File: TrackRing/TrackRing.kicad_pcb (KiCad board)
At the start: 2 copper layers, 12 x 15 mm, 7 parts, among them J1 Conn_01x04, U1 TLV493D-A1B6

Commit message: Finished BusChain PCB
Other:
- board text added: "TrackRing 1.1"
- board text added: "©CGR"
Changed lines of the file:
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@@
+    (effects (font (size 1 1) (thickness 0.15)) (justify left bottom mirror))
+  )
+  (gr_text "©CGR" (at 30.3 23.3) (layer "B.SilkS")
     (effects (font (size 1 1) (thickness 0.15)) (justify left bottom mirror))
   )
@@
     (effects (font (size 1 1) (thickness 0.15)) (justify left bottom mirror))
   )
+  (gr_text "TrackRing 1.1" (at 31.1 21.7) (layer "B.SilkS")
+    (effects (font (size 1 1) (thickness 0.15)) (justify left bottom mirror))
+  )

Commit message: Finalized PCBs for fabrication
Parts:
- added D1: LED, LED_SMD:LED_0603_1608Metric, F.Cu at (30.0, 32.0)
- added R5: 500, Resistor_SMD:R_0402_1005Metric, F.Cu at (31.5, 32.5)
- moved R3 1.01 mm to (28.5, 31.5)
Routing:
- net Net-(D1-K): track 0.00 -> 1.59 mm
- net /VCC: track 14.5 -> 15.5 mm
- net /SDA: track 9.33 -> 8.30 mm
- net GND: track 5.30 -> 6.29 mm, vias 4 -> 5
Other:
- board text added: "TrackRing 1.0"
- board text removed: "TrackRing 1.1"

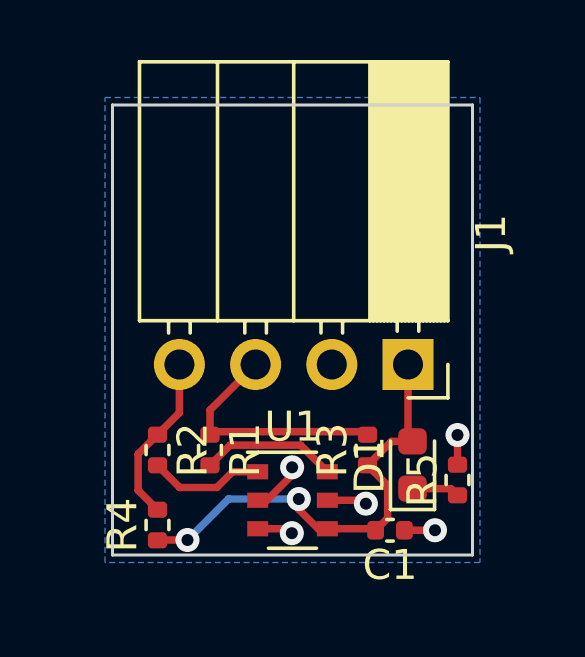
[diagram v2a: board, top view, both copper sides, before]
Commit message: Resolved various production and testing issues
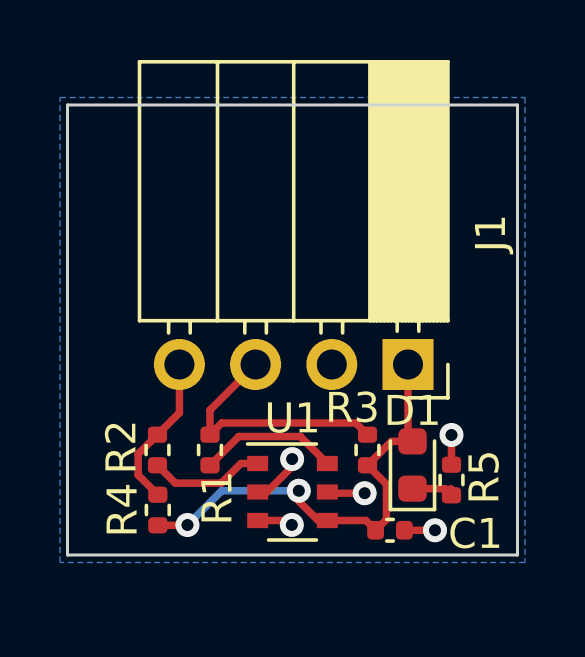
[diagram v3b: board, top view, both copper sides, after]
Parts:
- moved R4 0.50 mm to (21.5, 33.5)
- moved U1 0.27 mm to (26.0, 32.9)
- moved R5 0.20 mm to (31.3, 32.5)
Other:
- board size 12 x 15 mm -> 15 x 15 mm
